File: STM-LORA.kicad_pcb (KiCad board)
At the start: 2 copper layers, 56.5 x 50.8 mm, 58 parts, among them J1 Batt, J2 Solar, J3 CONN_01X17, J4 CONN_01X03, J5 CONN_01X03, J6 CONN_01X01, J7 CONN_01X14, J8 CONN_01X05, J9 CONN_01X05, U1 stm32f103c8t6-module-china, U2 RFM95HW

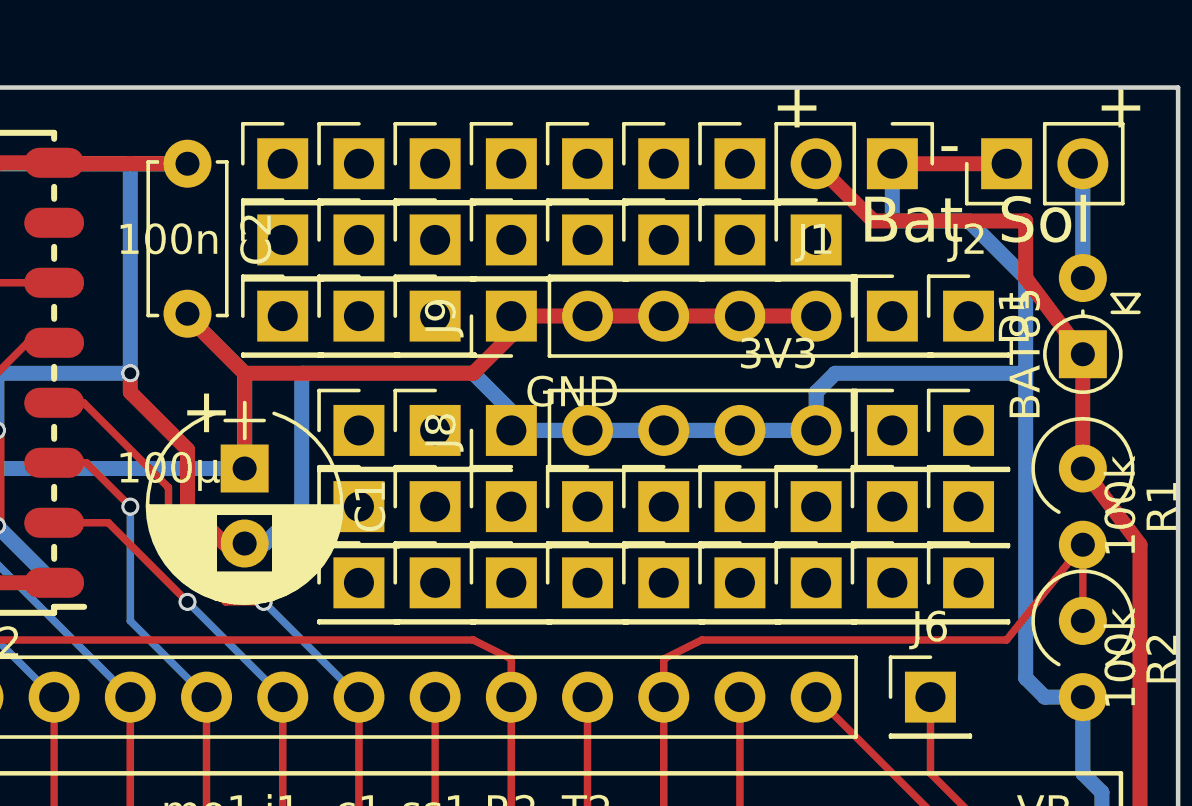
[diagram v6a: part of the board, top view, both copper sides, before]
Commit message: Change and add exp headers to schema (0.2)
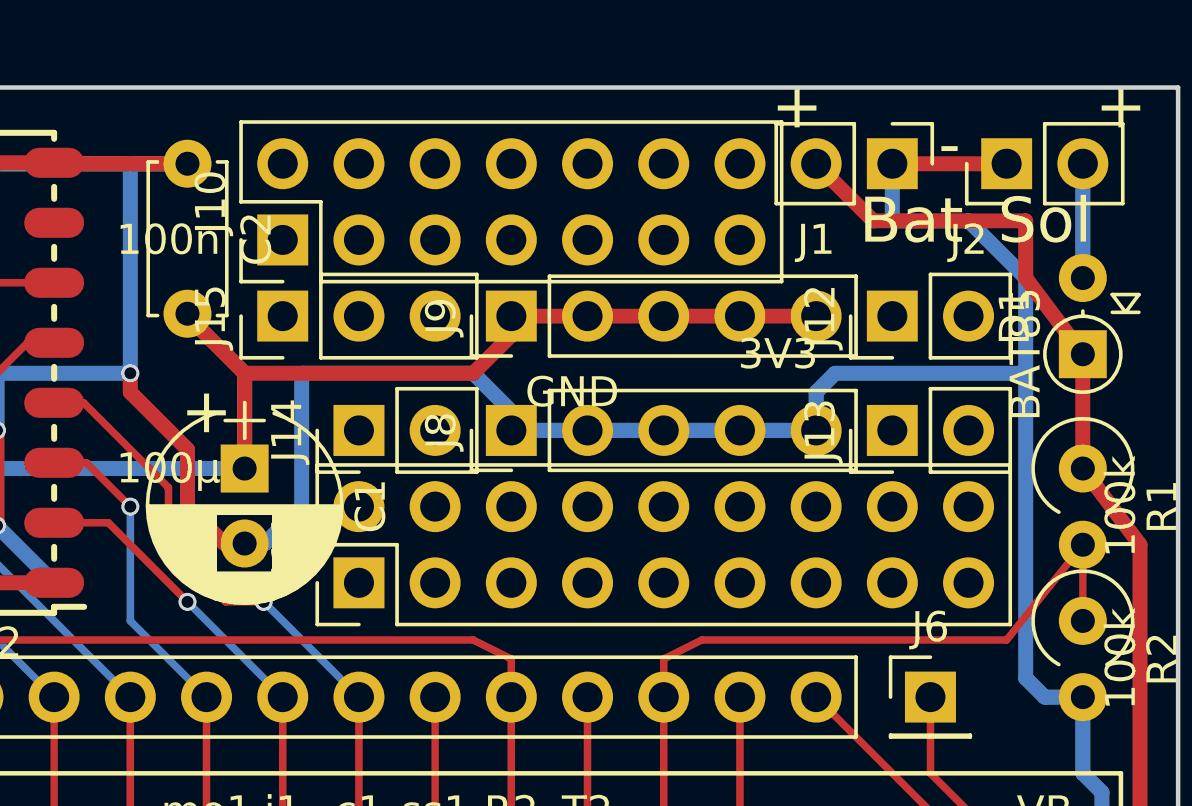
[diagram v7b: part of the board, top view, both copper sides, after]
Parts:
- removed ? (x42): Pin_Header_Straight_1x01_Pitch2.54mm, Pin_Headers:Pin_Header_Straight_1x01_Pitch2.54mm
- added J10: CONN_02X07, Pin_Headers:Pin_Header_Straight_2x07_Pitch2.54mm, F.Cu at (110.5, 61.0)
- added J11: CONN_02X09, Pin_Headers:Pin_Header_Straight_2x09_Pitch2.54mm, F.Cu at (113.0, 72.4)
- added J12: CONN_01X02, Pin_Headers:Pin_Header_Straight_1x02_Pitch2.54mm, F.Cu at (130.8, 63.5)
- added J13: CONN_01X02, Pin_Headers:Pin_Header_Straight_1x02_Pitch2.54mm, F.Cu at (130.8, 67.3)
- added J14: CONN_01X02, Pin_Headers:Pin_Header_Straight_1x02_Pitch2.54mm, F.Cu at (113.0, 67.3)
- added J15: CONN_01X03, Pin_Headers:Pin_Header_Straight_1x03_Pitch2.54mm, F.Cu at (110.5, 63.5)

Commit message: hide/clear connector labels
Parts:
- J10: value CONN_02X07 -> (none)
- J12, J14: value CONN_01X02 -> (none)
- J15, J5: value CONN_01X03 -> (none)
- J7: value CONN_01X14 -> (none)
- J8: value CONN_01X05 -> (none)
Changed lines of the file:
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@@
     (links 75)
     (no_connects 0)
-    (area 83.744999 54.656666 141.390371 109.173333)
+    (area 83.744999 55.315 141.390371 109.173333)
     (thickness 1.6)
     (drawings 20)
@@
     (aux_axis_origin 0 0)
     (grid_origin 83.82 55.88)
-    (visible_elements 7FFFBFFF)
+    (visible_elements 7FFFFFFF)
     (pcbplotparams
       (layerselection 0x010e0_80000001)
@@
       (effects (font (size 1 1) (thickness 0.15)))
     )
-    (fp_text value CONN_01X17 (at 0 42.97 270) (layer F.Fab)
+    (fp_text value CONN_01X17 (at 0 42.97 270) (layer F.Fab) hide
       (effects (font (size 1 1) (thickness 0.15)))
     )
@@
       (effects (font (size 1 1) (thickness 0.15)))
     )
-    (fp_text value CONN_01X03 (at 0 7.41 270) (layer F.Fab)
+    (fp_text value CONN_01X03 (at 0 7.41 270) (layer F.Fab) hide
       (effects (font (size 1 1) (thickness 0.15)))
     )
@@
       (effects (font (size 1 1) (thickness 0.15)))
     )
-    (fp_text value CONN_01X03 (at 0 7.41 90) (layer F.Fab)
+    (fp_text value "" (at 0 7.41 180) (layer F.Fab)
       (effects (font (size 1 1) (thickness 0.15)))
     )
@@
       (effects (font (size 1 1) (thickness 0.15)))
     )
-    (fp_text value CONN_01X01 (at 0 2.33) (layer F.Fab)
+    (fp_text value CONN_01X01 (at 0 2.33) (layer F.Fab) hide
       (effects (font (size 1 1) (thickness 0.15)))
     )
@@
       (effects (font (size 1 1) (thickness 0.15)))
     )
-    (fp_text value CONN_01X14 (at 0 35.35 90) (layer F.Fab)
+    (fp_text value "" (at 0 35.35 90) (layer F.Fab)
       (effects (font (size 1 1) (thickness 0.15)))
     )
@@
       (effects (font (size 1 1) (thickness 0.15)))
     )
-    (fp_text value CONN_01X05 (at 0 12.49 90) (layer F.Fab)
+    (fp_text value "" (at 0 12.49 90) (layer F.Fab)
       (effects (font (size 1 1) (thickness 0.15)))
     )
@@
       (effects (font (size 1 1) (thickness 0.15)))
     )
-    (fp_text value CONN_01X05 (at 0 12.49 90) (layer F.Fab)
+    (fp_text value CONN_01X05 (at 0 12.49 90) (layer F.Fab) hide
       (effects (font (size 1 1) (thickness 0.15)))
     )
@@
       (effects (font (size 1 1) (thickness 0.15)))
     )
-    (fp_text value CONN_02X07 (at 1.27 17.63 90) (layer F.Fab)
+    (fp_text value "" (at 1.27 17.63 90) (layer F.Fab)
       (effects (font (size 1 1) (thickness 0.15)))
     )
@@
       (effects (font (size 1 1) (thickness 0.15)))
     )
-    (fp_text value CONN_02X09 (at 1.27 22.71 90) (layer F.Fab)
+    (fp_text value CONN_02X09 (at 1.27 22.71 90) (layer F.Fab) hide
       (effects (font (size 1 1) (thickness 0.15)))
     )
@@
       (effects (font (size 1 1) (thickness 0.15)))
     )
-    (fp_text value CONN_01X02 (at 0 4.93 90) (layer F.Fab)
+    (fp_text value "" (at 0 4.93 90) (layer F.Fab)
       (effects (font (size 1 1) (thickness 0.15)))
     )
@@
       (effects (font (size 1 1) (thickness 0.15)))
     )
-    (fp_text value CONN_01X02 (at 0 4.93 90) (layer F.Fab)
+    (fp_text value CONN_01X02 (at 0 4.93 90) (layer F.Fab) hide
       (effects (font (size 1 1) (thickness 0.15)))
     )
@@
       (effects (font (size 1 1) (thickness 0.15)))
     )
-    (fp_text value CONN_01X02 (at 0 4.93 90) (layer F.Fab)
+    (fp_text value "" (at 0 4.93 90) (layer F.Fab)
       (effects (font (size 1 1) (thickness 0.15)))
     )
@@
       (effects (font (size 1 1) (thickness 0.15)))
     )
-    (fp_text value CONN_01X03 (at 0 7.47 90) (layer F.Fab)
-      (effects (font (size 1 1) (thickness 0.15)))
-    )
+    (fp_text value "" (at 0 7.47 90) (layer F.Fab)
+      (effects (font (size 1 1) (thickness 0.15)))
+    )
